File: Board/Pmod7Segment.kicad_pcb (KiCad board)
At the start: 2 copper layers, 97.8 x 15.2 mm, 19 parts, among them J1 PMOD

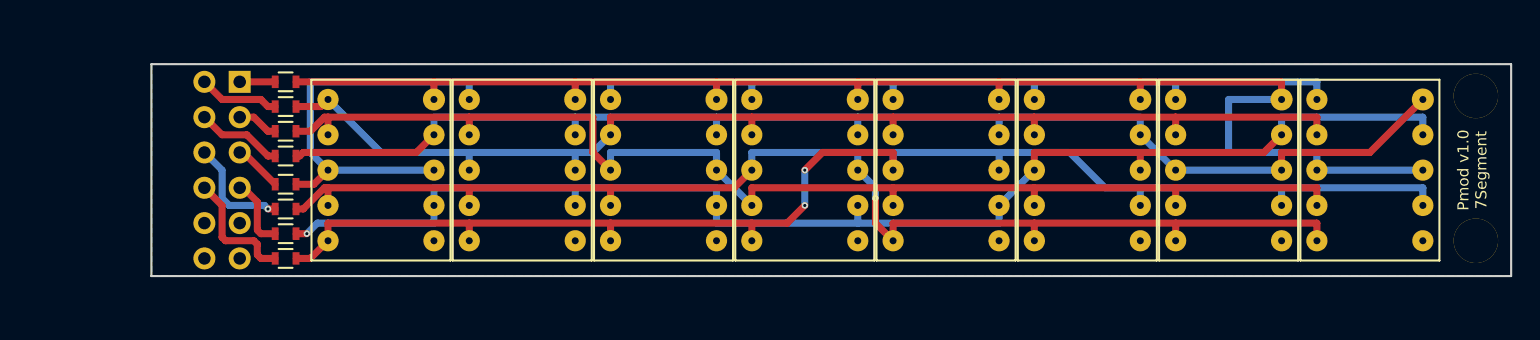
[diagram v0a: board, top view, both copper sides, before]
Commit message: Board resized
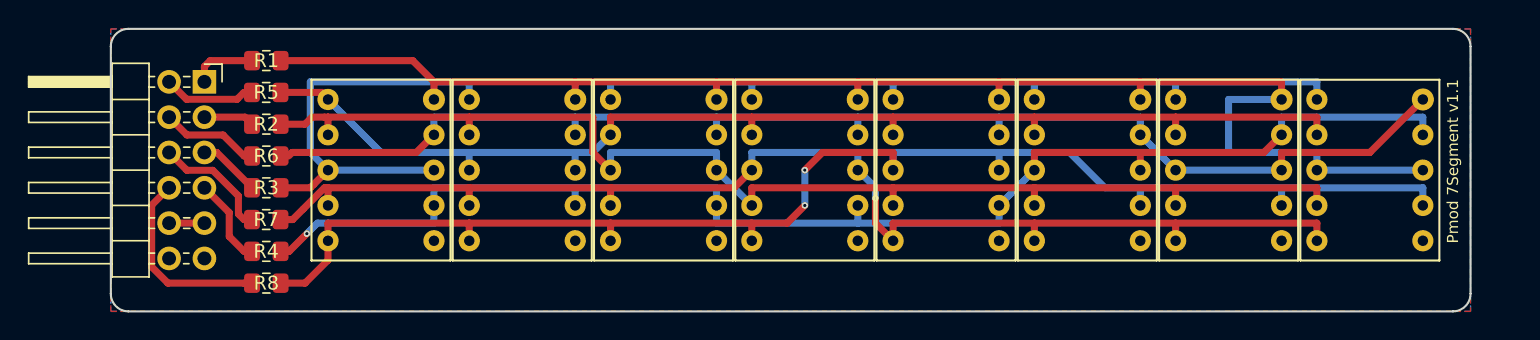
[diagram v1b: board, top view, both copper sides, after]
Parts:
- removed MOUNTING_HOLE_3-2MM_M3 (x2): VAL**, Mounting_Holes_Local:MOUNTING_HOLE_3-2MM_M3
- J1: footprint Digilent:PMOD-DUAL-MALE -> Kicad:PMODHeader_2x06_P2.54mm_Horizontal
- R1, R2, R3, R4, R5, R6, R7, R8: footprint Resistors_SMD:R_0603 -> Resistor_SMD:R_0805_2012Metric_Pad1.15x1.40mm_HandSolder
- moved J1 7.41 mm to (105.4, 82.5), turned to 180 degrees
- moved R8 2.26 mm to (109.9, 84.3)
- moved R1 2.06 mm to (109.9, 68.3)
- moved R4 1.88 mm to (109.9, 82.0)
- moved R5 1.73 mm to (109.9, 70.6)
- moved R7 1.59 mm to (109.9, 79.8)
- moved R2 1.48 mm to (109.9, 72.9)
- moved R3 1.41 mm to (109.9, 77.5)
- moved R6 1.39 mm to (109.9, 75.2)
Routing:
- net Net-(J1-Pad10): track 8.98 -> 13.9 mm
- net /S3: track 98.9 -> 101.6 mm
- net GND: track 0.00 -> 2.54 mm
- net Net-(J1-Pad1): track 2.55 -> 4.96 mm
- net /S0: track 102.6 -> 104.4 mm
- net /S2: track 96.9 -> 98.5 mm
- net /S4: track 89.6 -> 91.0 mm
- net Net-(J1-Pad4): track 5.11 -> 6.33 mm
- net /S7: track 98.5 -> 99.7 mm
- net /S6: track 85.9 -> 87.1 mm
- net /S1: track 93.2 -> 94.3 mm
- net Net-(J1-Pad9): track 7.97 -> 8.97 mm, vias 1 -> 0
- net Net-(J1-Pad3): track 3.50 -> 4.48 mm
- net /S5: track 89.4 -> 90.3 mm
- net Net-(J1-Pad8): track 6.25 -> 7.13 mm
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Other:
- board size 97.8 x 15.2 mm -> 97.8 x 20.3 mm
- net class Double added: clearance 0.1524, trace_width 0.508, via_dia 0.4572, via_drill 0.3048
- board text added: "Pmod 7Segment v1.1"
- board text removed: "Pmod v1.0 7Segment"

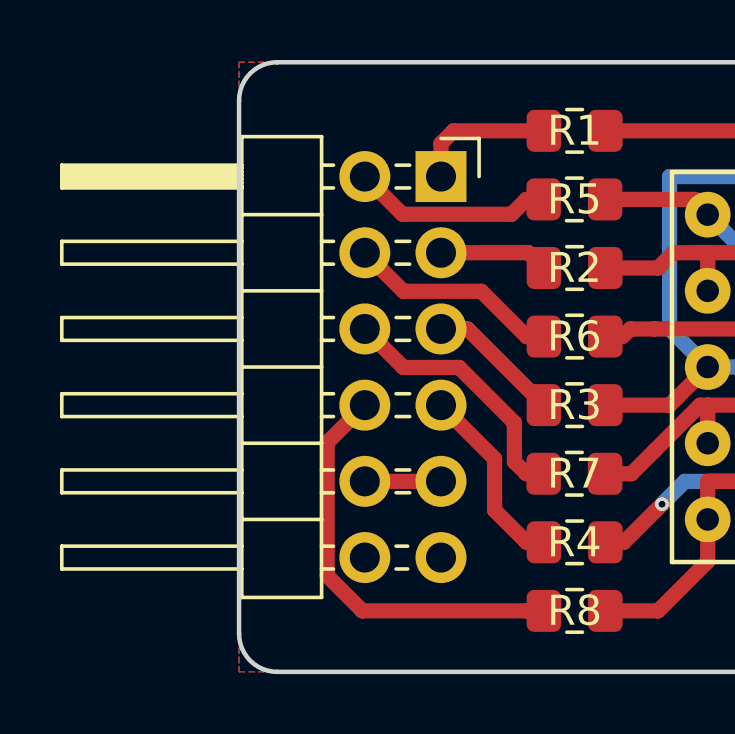
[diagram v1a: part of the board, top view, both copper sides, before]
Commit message: Placeholder for Ordernumber added
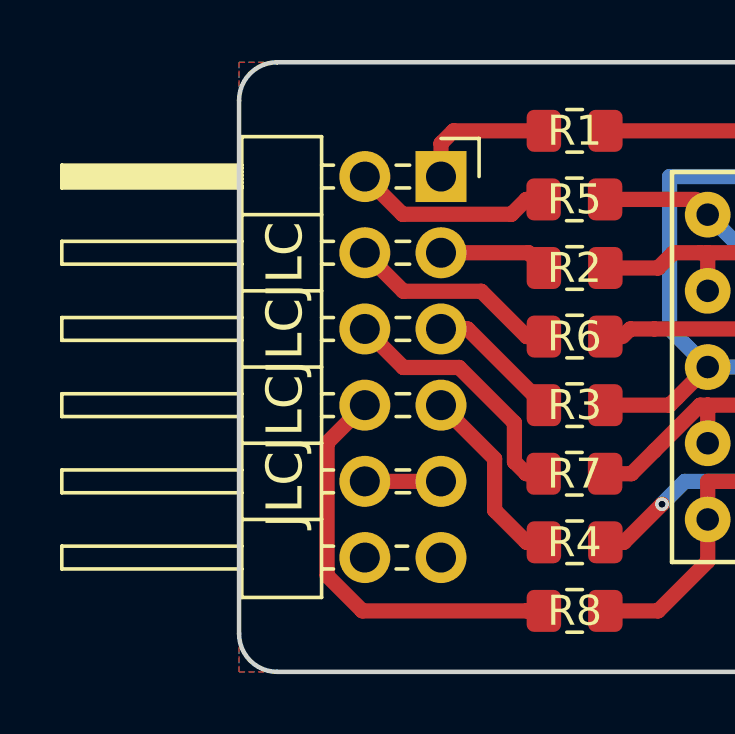
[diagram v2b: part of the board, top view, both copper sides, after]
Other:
- board text added: "JLCJLCJLCJLC"
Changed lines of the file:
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@@
   (general
     (thickness 1.6)
-    (drawings 13)
+    (drawings 14)
     (tracks 224)
     (zones 0)
@@
       (net 17 /S1))
   )
+  (gr_text JLCJLCJLCJLC (at 100.203 76.454 90) (layer F.SilkS)
+    (effects (font (size 1.2 1.2) (thickness 0.15)))
+  )
   (dimension 97.79 (width 0.15) (layer F.SilkS)
